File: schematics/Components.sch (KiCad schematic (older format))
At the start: 7 parts

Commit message: Change footprint of LD1117
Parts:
- U?: footprint Package_TO_SOT_SMD:SOT-223-3_TabPin2 -> Package_TO_SOT_THT:TO-220-3_Horizontal_TabUp
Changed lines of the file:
@@
 F 0 "U?" V 4196 2955 50  0000 L CNN
 F 1 "LD1117_3V3" V 4105 2955 50  0000 L CNN
-F 2 "Package_TO_SOT_SMD:SOT-223-3_TabPin2" H 4150 3050 50  0001 C CNN
+F 2 "Package_TO_SOT_THT:TO-220-3_Horizontal_TabUp" H 4150 3050 50  0001 C CNN
 F 3 "http://www.st.com/st-web-ui/static/active/en/resource/technical/document/datasheet/CD00000544.pdf" H 4250 2600 50  0001 C CNN
 	1    4150 2850

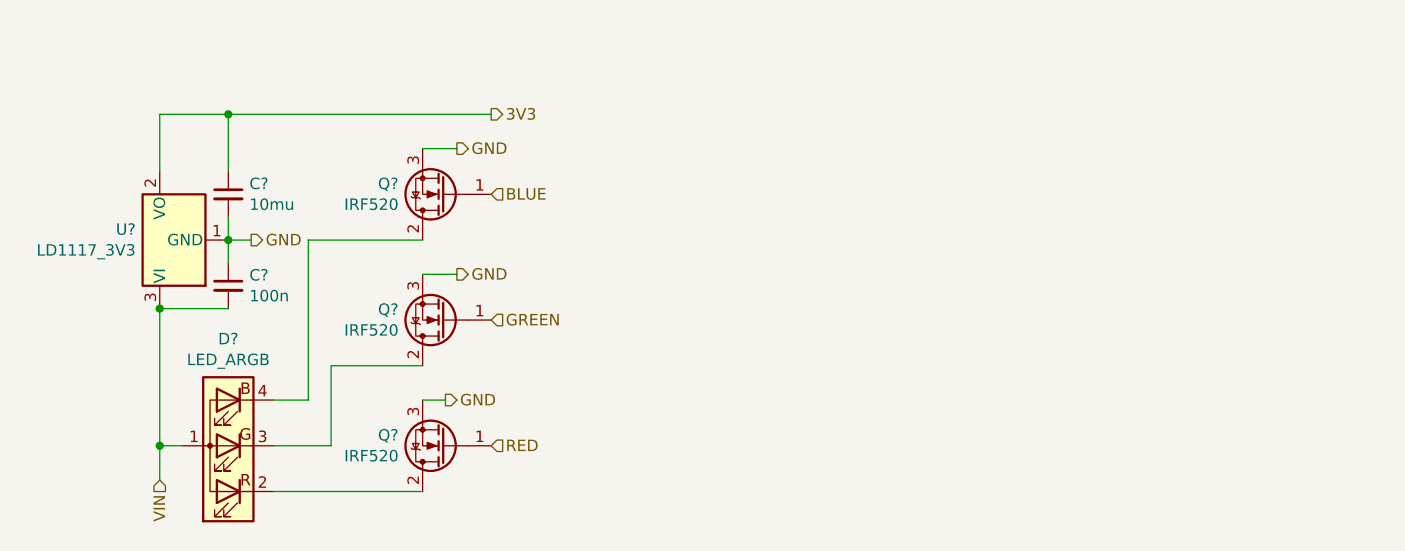
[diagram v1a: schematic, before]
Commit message: Change MOSFET, annotate schematics
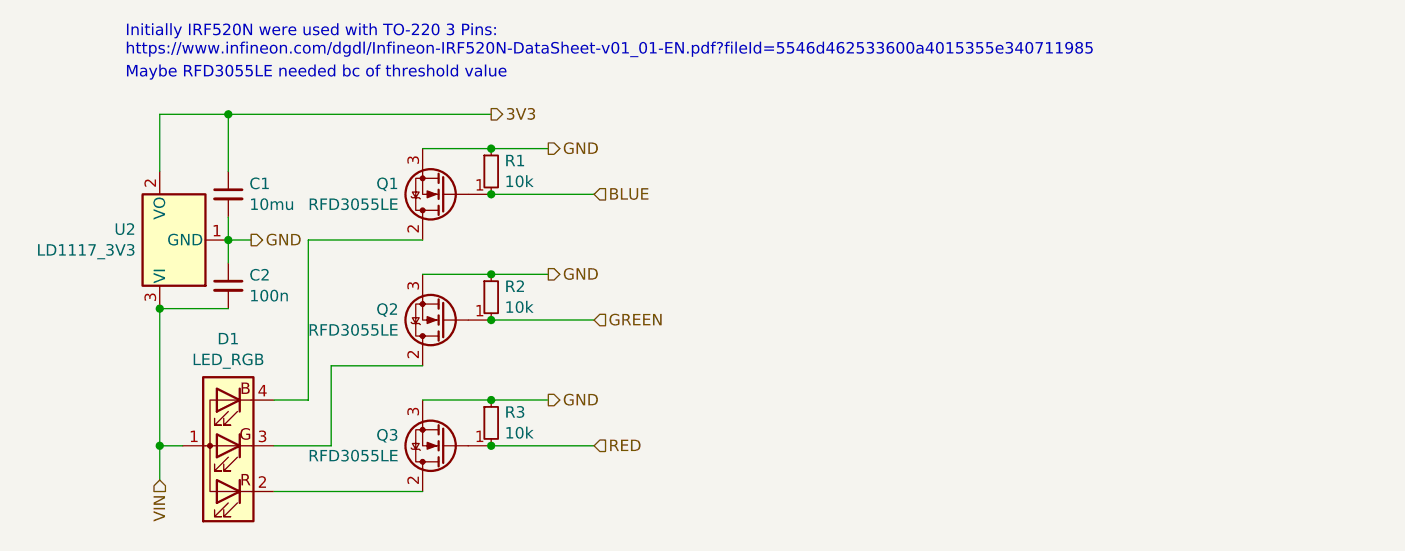
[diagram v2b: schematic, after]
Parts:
- added R1, R2, R3: 10k, symbol Device:R_Small
- D1: renamed from D?; value LED_ARGB -> LED_RGB
- Q1, Q2, Q3: renamed from Q?; value IRF520 -> RFD3055LE; footprint Package_TO_SOT_THT:TO-220-3_Vertical -> Package_TO_SOT_THT:TO-251-3_Vertical
- gave numbers to parts that had none: 3
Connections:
- net BLUE: now also R1.2
- net GND: now also R1.1, R2.1, R3.1
- net GREEN: now also R2.2
- net RED: now also R3.2
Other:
- note added: "Initially IRF520N were used with TO-220 3 Pins:\nhttps://www.infineon.com/dgdl/Infineon-IRF520N-DataSheet-v01_01-EN.pdf?fileId=5546d462533600a4015355e340711985"
- note added: "Maybe RFD3055LE needed bc of threshold value"
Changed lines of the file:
@@
 $EndDescr
 $Comp
-L Regulator_Linear:LD1117S33TR_SOT223 U?
+L Regulator_Linear:LD1117S33TR_SOT223 U2
 U 1 1 60EFA784
 P 4150 2850
-F 0 "U?" V 4196 2955 50  0000 L CNN
+F 0 "U2" V 4196 2955 50  0000 L CNN
 F 1 "LD1117_3V3" V 4105 2955 50  0000 L CNN
 F 2 "Package_TO_SOT_THT:TO-220-3_Horizontal_TabUp" H 4150 3050 50  0001 C CNN
@@
 $EndComp
 $Comp
-L Transistor_FET:IRF540N Q?
+L Transistor_FET:IRF540N Q3
 U 1 1 60F024FB
 P 5400 3750
-F 0 "Q?" H 5605 3704 50  0000 L CNN
-F 1 "IRF520" H 5605 3795 50  0000 L CNN
-F 2 "Package_TO_SOT_THT:TO-220-3_Vertical" H 5650 3675 50  0001 L CIN
-F 3 "http://www.irf.com/product-info/datasheets/data/irf540n.pdf" H 5400 3750 50  0001 L CNN
+F 0 "Q3" H 5605 3704 50  0000 L CNN
+F 1 "RFD3055LE" H 5605 3795 50  0000 L CNN
+F 2 "Package_TO_SOT_THT:TO-251-3_Vertical" H 5650 3675 50  0001 L CIN
+F 3 "https://www.mouser.com/datasheet/2/308/1/RFD3055LESM_D-2319857.pdf" H 5400 3750 50  0001 L CNN
 	1    5400 3750
 	-1   0    0    1
 $EndComp
 $Comp
-L Transistor_FET:IRF540N Q?
+L Transistor_FET:IRF540N Q2
 U 1 1 60F03EB6
 P 5400 3200
-F 0 "Q?" H 5605 3154 50  0000 L CNN
-F 1 "IRF520" H 5605 3245 50  0000 L CNN
-F 2 "Package_TO_SOT_THT:TO-220-3_Vertical" H 5650 3125 50  0001 L CIN
-F 3 "http://www.irf.com/product-info/datasheets/data/irf540n.pdf" H 5400 3200 50  0001 L CNN
+F 0 "Q2" H 5605 3154 50  0000 L CNN
+F 1 "RFD3055LE" H 5605 3245 50  0000 L CNN
+F 2 "Package_TO_SOT_THT:TO-251-3_Vertical" H 5650 3125 50  0001 L CIN
+F 3 "https://www.mouser.com/datasheet/2/308/1/RFD3055LESM_D-2319857.pdf" H 5400 3200 50  0001 L CNN
 	1    5400 3200
 	-1   0    0    1
 $EndComp
 $Comp
-L Transistor_FET:IRF540N Q?
+L Transistor_FET:IRF540N Q1
 U 1 1 60F0615A
 P 5400 2650
-F 0 "Q?" H 5605 2604 50  0000 L CNN
-F 1 "IRF520" H 5605 2695 50  0000 L CNN
-F 2 "Package_TO_SOT_THT:TO-220-3_Vertical" H 5650 2575 50  0001 L CIN
-F 3 "http://www.irf.com/product-info/datasheets/data/irf540n.pdf" H 5400 2650 50  0001 L CNN
+F 0 "Q1" H 5605 2604 50  0000 L CNN
+F 1 "RFD3055LE" H 5605 2695 50  0000 L CNN
+F 2 "Package_TO_SOT_THT:TO-251-3_Vertical" H 5650 2575 50  0001 L CIN
+F 3 "https://www.mouser.com/datasheet/2/308/1/RFD3055LESM_D-2319857.pdf" H 5400 2650 50  0001 L CNN
 	1    5400 2650
 	-1   0    0    1
@@
 	4900 3400 5300 3400
 Wire Wire Line
-	4650 3550 4800 3550
-Wire Wire Line
-	4800 3550 4800 2850
-Wire Wire Line
-	4800 2850 5300 2850
-Wire Wire Line
 	4150 3750 4250 3750
 Wire Wire Line
@@
 	4150 2300 4450 2300
 $Comp
-L Device:C_Small C?
+L Device:C_Small C1
 U 1 1 60F33F39
 P 4450 2650
-F 0 "C?" H 4542 2696 50  0000 L CNN
+F 0 "C1" H 4542 2696 50  0000 L CNN
 F 1 "10mu" H 4542 2605 50  0000 L CNN
 F 2 "" H 4450 2650 50  0001 C CNN
@@
 $EndComp
 $Comp
-L Device:C_Small C?
+L Device:C_Small C2
 U 1 1 60F35104
 P 4450 3050
-F 0 "C?" H 4542 3096 50  0000 L CNN
+F 0 "C2" H 4542 3096 50  0000 L CNN
 F 1 "100n" H 4542 3005 50  0000 L CNN
 F 2 "" H 4450 3050 50  0001 C CNN
@@
 Connection ~ 4450 2850
 $Comp
-L Device:LED_ARGB D?
+L Device:LED_ARGB D1
 U 1 1 60F08554
 P 4450 3750
-F 0 "D?" H 4450 3283 50  0000 C CNN
-F 1 "LED_ARGB" H 4450 3374 50  0000 C CNN
+F 0 "D1" H 4450 3283 50  0000 C CNN
+F 1 "LED_RGB" H 4450 3374 50  0000 C CNN
 F 2 "" H 4450 3700 50  0001 C CNN
 F 3 "~" H 4450 3700 50  0001 C CNN
@@
 	-1   0    0    1
 $EndComp
-Text HLabel 5600 3750 2    50   Input ~ 0
+Text HLabel 6050 3750 2    50   Input ~ 0
 RED
-Text HLabel 5600 3200 2    50   Input ~ 0
+Text HLabel 6050 3200 2    50   Input ~ 0
 GREEN
-Text HLabel 5600 2650 2    50   Input ~ 0
+Text HLabel 6050 2650 2    50   Input ~ 0
 BLUE
 Text HLabel 5600 2300 2    50   Output ~ 0
@@
 Wire Wire Line
 	4550 2850 4450 2850
-Text HLabel 5400 3550 2    50   Output ~ 0
+Text HLabel 5850 3550 2    50   Output ~ 0
 GND
-Text HLabel 5450 3000 2    50   Output ~ 0
+Text HLabel 5850 3000 2    50   Output ~ 0
 GND
-Text HLabel 5450 2450 2    50   Output ~ 0
+Text HLabel 5850 2450 2    50   Output ~ 0
 GND
-Wire Wire Line
-	5300 3550 5400 3550
-Wire Wire Line
-	5450 3000 5300 3000
-Wire Wire Line
-	5450 2450 5300 2450
 Text HLabel 4150 3900 3    50   Input ~ 0
 VIN
@@
 	4150 3900 4150 3750
 Connection ~ 4150 3750
+Text Notes 4000 2150 0    50   ~ 0
+Maybe RFD3055LE needed bc of threshold value
+Text Notes 4000 2050 0    50   ~ 0
+Initially IRF520N were used with TO-220 3 Pins:\nhttps://www.infineon.com/dgdl/Infineon-IRF520N-DataSheet-v01_01-EN.pdf?fileId=5546d462533600a4015355e340711985
+Wire Wire Line
+	4800 2850 5300 2850
+Wire Wire Line
+	4650 3550 4800 3550
+Wire Wire Line
+	4800 3550 4800 2850
+$Comp
+L Device:R_Small R1
+U 1 1 60F1E580
+P 5600 2550
+F 0 "R1" H 5659 2596 50  0000 L CNN
+F 1 "10k" H 5659 2505 50  0000 L CNN
+F 2 "" H 5600 2550 50  0001 C CNN
+F 3 "~" H 5600 2550 50  0001 C CNN
+	1    5600 2550
+	1    0    0    -1
+$EndComp
+$Comp
+L Device:R_Small R2
+U 1 1 60F1ED74
+P 5600 3100
+F 0 "R2" H 5659 3146 50  0000 L CNN
+F 1 "10k" H 5659 3055 50  0000 L CNN
+F 2 "" H 5600 3100 50  0001 C CNN
+F 3 "~" H 5600 3100 50  0001 C CNN
+	1    5600 3100
+	1    0    0    -1
+$EndComp
+$Comp
+L Device:R_Small R3
+U 1 1 60F1F2AA
+P 5600 3650
+F 0 "R3" H 5659 3696 50  0000 L CNN
+F 1 "10k" H 5659 3605 50  0000 L CNN
+F 2 "" H 5600 3650 50  0001 C CNN
+F 3 "~" H 5600 3650 50  0001 C CNN
+	1    5600 3650
+	1    0    0    -1
+$EndComp
+Wire Wire Line
+	5300 3550 5600 3550
+Connection ~ 5600 3550
+Wire Wire Line
+	5600 3550 5850 3550
+Wire Wire Line
+	6050 3750 5600 3750
+Connection ~ 5600 3750
+Wire Wire Line
+	6050 3200 5600 3200
+Connection ~ 5600 3200
+Wire Wire Line
+	5300 3000 5600 3000
+Connection ~ 5600 3000
+Wire Wire Line
+	5600 3000 5850 3000
+Wire Wire Line
+	6050 2650 5600 2650
+Connection ~ 5600 2650
+Wire Wire Line
+	5300 2450 5600 2450
+Connection ~ 5600 2450
+Wire Wire Line
+	5600 2450 5850 2450
 $EndSCHEMATC

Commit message: Assign footprints
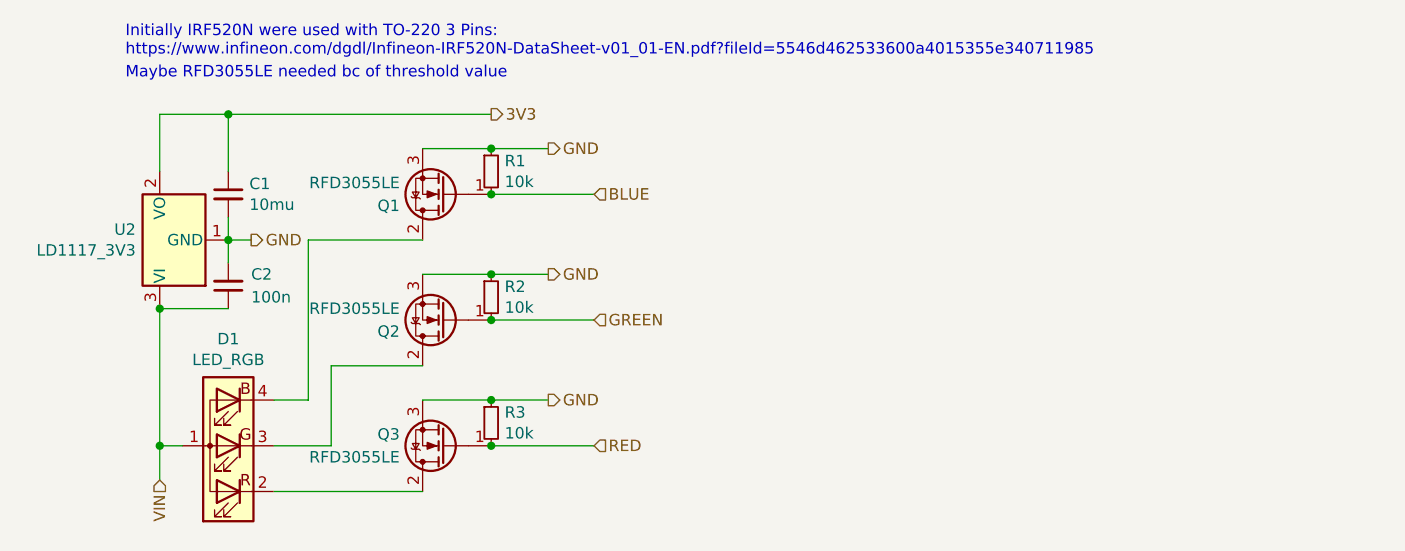
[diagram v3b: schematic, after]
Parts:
- C1: footprint (none) -> Capacitor_THT:CP_Radial_D6.3mm_P2.50mm
- C2: footprint (none) -> Capacitor_THT:C_Disc_D7.0mm_W2.5mm_P5.00mm
- D1: footprint (none) -> Connector_PinHeader_2.54mm:PinHeader_1x04_P2.54mm_Vertical
- R1, R2, R3: footprint (none) -> Resistor_THT:R_Axial_DIN0207_L6.3mm_D2.5mm_P5.08mm_Vertical
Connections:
- net GND: now also C2.2; no longer C2.1
- net VIN: now also C2.1; no longer C2.2
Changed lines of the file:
@@
 U 1 1 60F024FB
 P 5400 3750
-F 0 "Q3" H 5605 3704 50  0000 L CNN
-F 1 "RFD3055LE" H 5605 3795 50  0000 L CNN
+F 0 "Q3" H 5600 3700 50  0000 L CNN
+F 1 "RFD3055LE" H 5600 3800 50  0000 L CNN
 F 2 "Package_TO_SOT_THT:TO-251-3_Vertical" H 5650 3675 50  0001 L CIN
 F 3 "https://www.mouser.com/datasheet/2/308/1/RFD3055LESM_D-2319857.pdf" H 5400 3750 50  0001 L CNN
@@
 U 1 1 60F03EB6
 P 5400 3200
-F 0 "Q2" H 5605 3154 50  0000 L CNN
-F 1 "RFD3055LE" H 5605 3245 50  0000 L CNN
+F 0 "Q2" H 5600 3250 50  0000 L CNN
+F 1 "RFD3055LE" H 5600 3150 50  0000 L CNN
 F 2 "Package_TO_SOT_THT:TO-251-3_Vertical" H 5650 3125 50  0001 L CIN
 F 3 "https://www.mouser.com/datasheet/2/308/1/RFD3055LESM_D-2319857.pdf" H 5400 3200 50  0001 L CNN
@@
 U 1 1 60F0615A
 P 5400 2650
-F 0 "Q1" H 5605 2604 50  0000 L CNN
-F 1 "RFD3055LE" H 5605 2695 50  0000 L CNN
+F 0 "Q1" H 5600 2700 50  0000 L CNN
+F 1 "RFD3055LE" H 5600 2600 50  0000 L CNN
 F 2 "Package_TO_SOT_THT:TO-251-3_Vertical" H 5650 2575 50  0001 L CIN
 F 3 "https://www.mouser.com/datasheet/2/308/1/RFD3055LESM_D-2319857.pdf" H 5400 2650 50  0001 L CNN
@@
 F 0 "C1" H 4542 2696 50  0000 L CNN
 F 1 "10mu" H 4542 2605 50  0000 L CNN
-F 2 "" H 4450 2650 50  0001 C CNN
+F 2 "Capacitor_THT:CP_Radial_D6.3mm_P2.50mm" H 4450 2650 50  0001 C CNN
 F 3 "~" H 4450 2650 50  0001 C CNN
 	1    4450 2650
@@
 U 1 1 60F35104
 P 4450 3050
-F 0 "C2" H 4542 3096 50  0000 L CNN
-F 1 "100n" H 4542 3005 50  0000 L CNN
-F 2 "" H 4450 3050 50  0001 C CNN
+F 0 "C2" H 4350 3000 50  0000 R CNN
+F 1 "100n" H 4350 3100 50  0000 R CNN
+F 2 "Capacitor_THT:C_Disc_D7.0mm_W2.5mm_P5.00mm" H 4450 3050 50  0001 C CNN
 F 3 "~" H 4450 3050 50  0001 C CNN
 	1    4450 3050
-	1    0    0    -1
+	-1   0    0    1
 $EndComp
 Wire Wire Line
@@
 F 0 "D1" H 4450 3283 50  0000 C CNN
 F 1 "LED_RGB" H 4450 3374 50  0000 C CNN
-F 2 "" H 4450 3700 50  0001 C CNN
+F 2 "Connector_PinHeader_2.54mm:PinHeader_1x04_P2.54mm_Vertical" H 4450 3700 50  0001 C CNN
 F 3 "~" H 4450 3700 50  0001 C CNN
 	1    4450 3750
@@
 F 0 "R1" H 5659 2596 50  0000 L CNN
 F 1 "10k" H 5659 2505 50  0000 L CNN
-F 2 "" H 5600 2550 50  0001 C CNN
+F 2 "Resistor_THT:R_Axial_DIN0207_L6.3mm_D2.5mm_P5.08mm_Vertical" H 5600 2550 50  0001 C CNN
 F 3 "~" H 5600 2550 50  0001 C CNN
 	1    5600 2550
@@
 F 0 "R2" H 5659 3146 50  0000 L CNN
 F 1 "10k" H 5659 3055 50  0000 L CNN
-F 2 "" H 5600 3100 50  0001 C CNN
+F 2 "Resistor_THT:R_Axial_DIN0207_L6.3mm_D2.5mm_P5.08mm_Vertical" H 5600 3100 50  0001 C CNN
 F 3 "~" H 5600 3100 50  0001 C CNN
 	1    5600 3100
@@
 F 0 "R3" H 5659 3696 50  0000 L CNN
 F 1 "10k" H 5659 3605 50  0000 L CNN
-F 2 "" H 5600 3650 50  0001 C CNN
+F 2 "Resistor_THT:R_Axial_DIN0207_L6.3mm_D2.5mm_P5.08mm_Vertical" H 5600 3650 50  0001 C CNN
 F 3 "~" H 5600 3650 50  0001 C CNN
 	1    5600 3650
